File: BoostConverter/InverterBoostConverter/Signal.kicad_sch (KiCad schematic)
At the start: 58 parts, among them IC4 LM358DR, IC5 LM358DR, IC6 MCP2515-e_ST, IC7 TJA1050T_CM,118, SW1 SW_Push, U2 TL431AIDBZR, U4 TMP36xS, U5 TMP36xS, Y1 8MHz

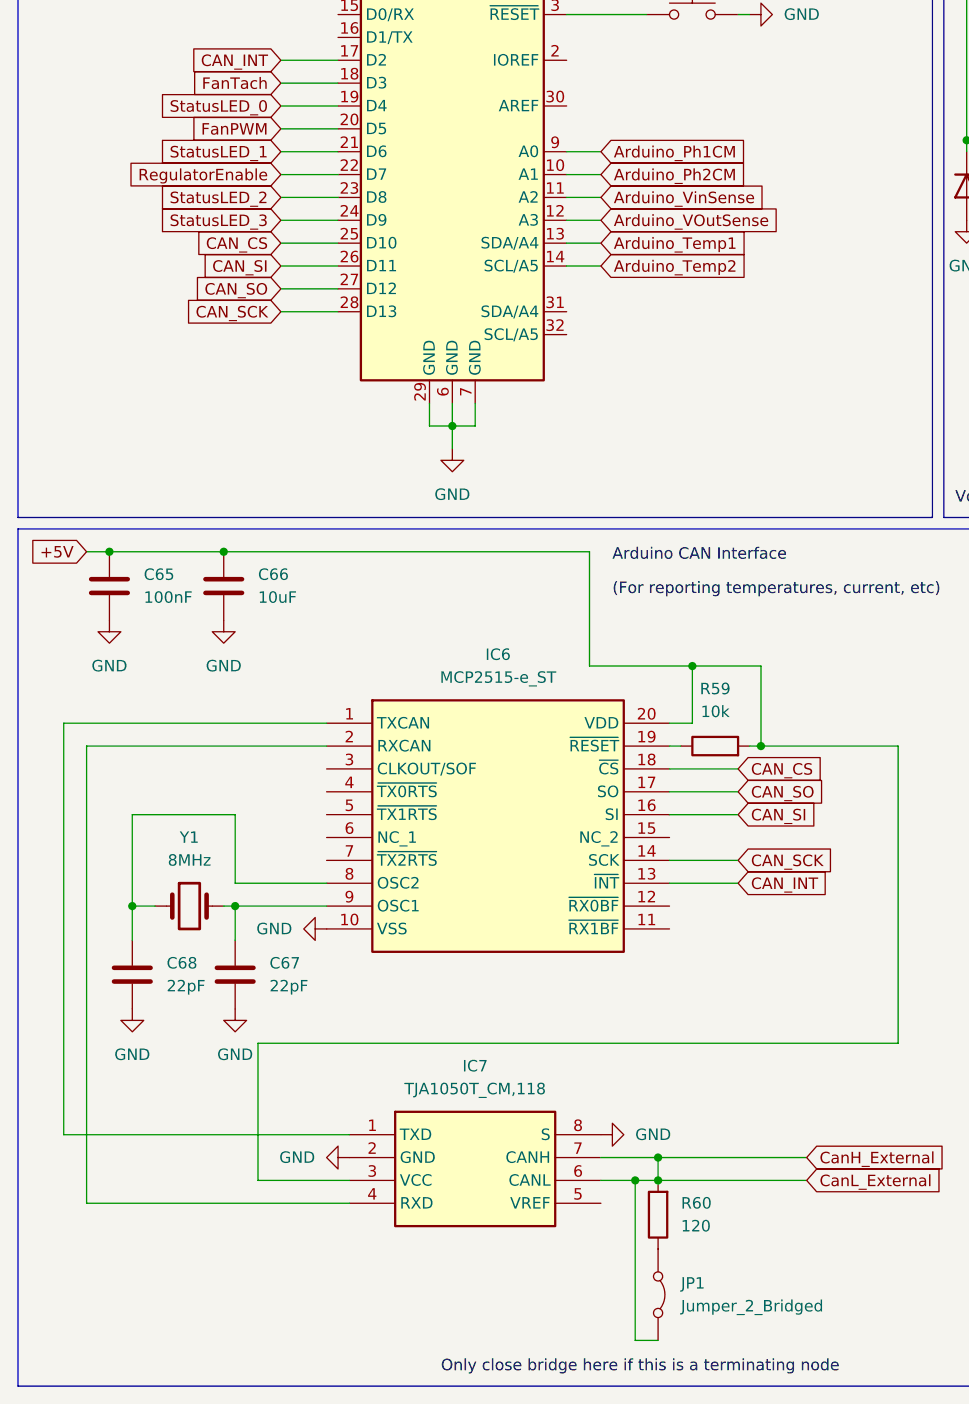
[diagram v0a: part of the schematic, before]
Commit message: Update boost converter, add inverter
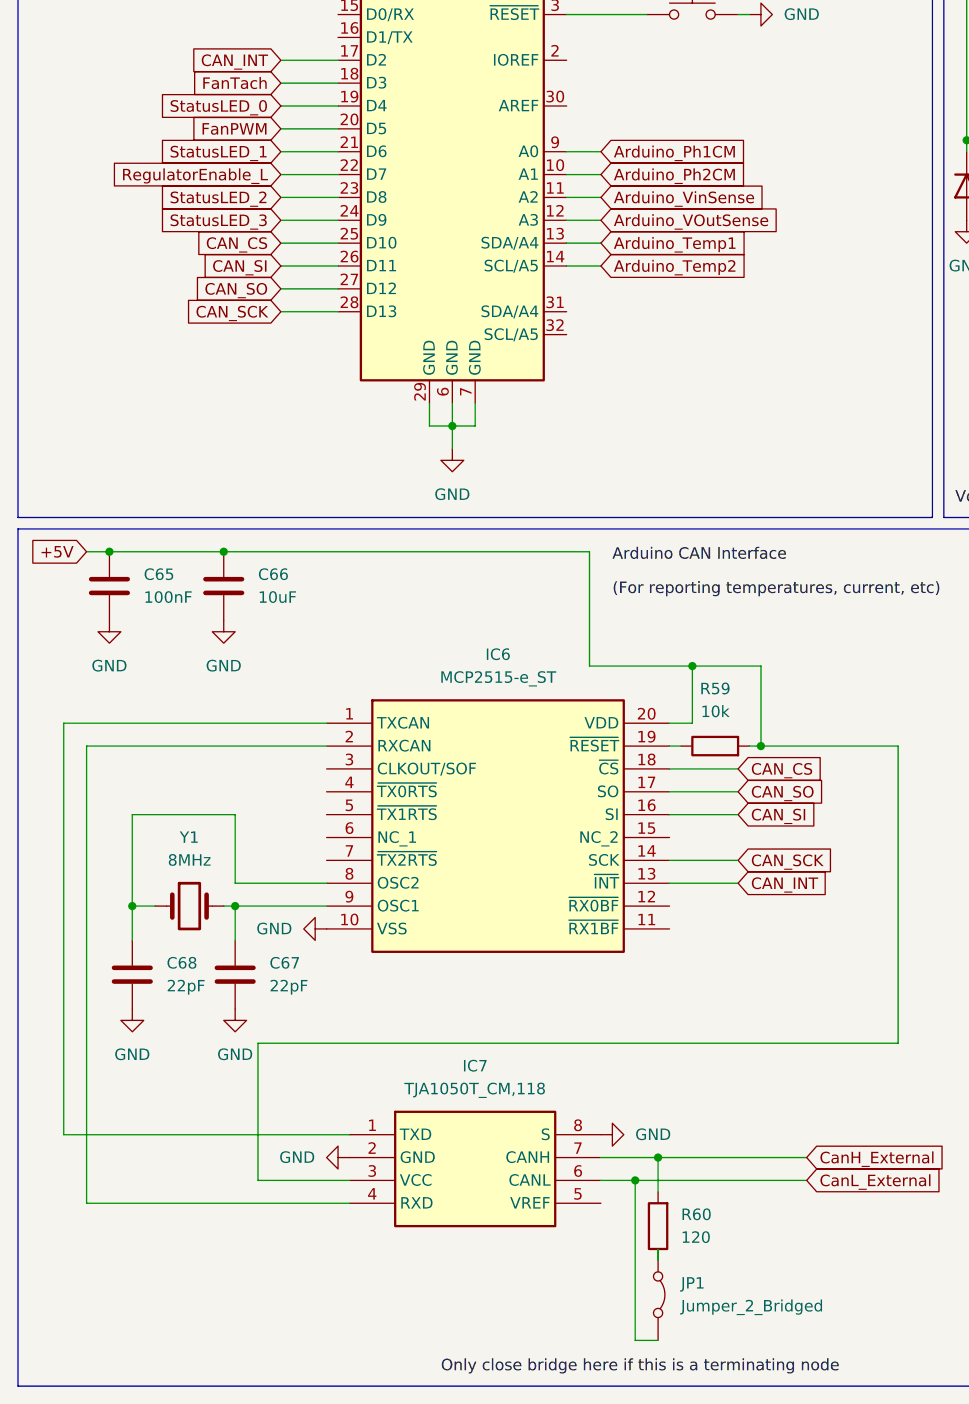
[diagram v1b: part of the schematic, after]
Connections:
- net CanH_External: no longer IC7.6 (CANL), JP1.2 (B)
- net RegulatorEnable renamed RegulatorEnable_L
- new net CanL_External: IC7.6 (CANL), JP1.2 (B)
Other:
- moved on the sheet: R60
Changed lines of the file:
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@@
 	)
 	(junction
-		(at 85.09 173.99)
-		(diameter 0)
-		(color 0 0 0 0)
-	)
-	(junction
 		(at 246.38 48.26)
 		(diameter 0)
@@
 	)
 	(junction
+		(at 85.09 171.45)
+		(diameter 0)
+		(color 0 0 0 0)
+	)
+	(junction
 		(at 278.13 48.26)
 		(diameter 0)
@@
 		(color 0 0 0 0)
 	)
-	(junction
-		(at 85.09 171.45)
-		(diameter 0)
-		(color 0 0 0 0)
-	)
 	(wire
 		(pts
@@
 	(wire
 		(pts
-			(xy 85.09 173.99) (xy 101.6 173.99)
-		)
-		(stroke
-			(width 0)
-			(type default)
-		)
-	)
-	(wire
-		(pts
 			(xy 78.74 17.78) (xy 91.44 17.78)
 		)
@@
 	(wire
 		(pts
+			(xy 85.09 171.45) (xy 101.6 171.45)
+		)
+		(stroke
+			(width 0)
+			(type default)
+		)
+	)
+	(wire
+		(pts
 			(xy 74.93 67.31) (xy 78.74 67.31)
 		)
@@
 	(wire
 		(pts
-			(xy 82.55 173.99) (xy 85.09 173.99)
+			(xy 82.55 173.99) (xy 101.6 173.99)
 		)
 		(stroke
@@
 	(wire
 		(pts
+			(xy 85.09 171.45) (xy 85.09 175.26)
+		)
+		(stroke
+			(width 0)
+			(type default)
+		)
+	)
+	(wire
+		(pts
 			(xy 43.18 57.15) (xy 49.53 57.15)
 		)
@@
 	(wire
 		(pts
-			(xy 85.09 171.45) (xy 101.6 171.45)
-		)
-		(stroke
-			(width 0)
-			(type default)
-		)
-	)
-	(wire
-		(pts
 			(xy 191.77 123.19) (xy 195.58 123.19)
 		)
@@
 	(wire
 		(pts
-			(xy 85.09 171.45) (xy 85.09 173.99)
+			(xy 129.54 52.07) (xy 129.54 58.42)
 		)
 		(stroke
@@
 	(wire
 		(pts
-			(xy 129.54 52.07) (xy 129.54 58.42)
+			(xy 193.04 134.62) (xy 195.58 134.62)
 		)
 		(stroke
@@
 	(wire
 		(pts
-			(xy 193.04 134.62) (xy 195.58 134.62)
+			(xy 156.21 125.73) (xy 158.75 125.73)
 		)
 		(stroke
@@
 	(wire
 		(pts
-			(xy 156.21 125.73) (xy 158.75 125.73)
+			(xy 180.34 36.83) (xy 180.34 60.96)
 		)
 		(stroke
@@
 	(wire
 		(pts
-			(xy 180.34 36.83) (xy 180.34 60.96)
+			(xy 236.22 123.19) (xy 240.03 123.19)
 		)
 		(stroke
@@
 	(wire
 		(pts
-			(xy 236.22 123.19) (xy 240.03 123.19)
+			(xy 21.59 104.14) (xy 24.13 104.14)
 		)
 		(stroke
@@
 	(wire
 		(pts
-			(xy 21.59 104.14) (xy 24.13 104.14)
+			(xy 85.09 182.88) (xy 85.09 181.61)
 		)
 		(stroke
@@
 		)
 	)
-	(global_label "RegulatorEnable"
-		(shape input)
-		(at 43.18 62.23 180)
-		(fields_autoplaced yes)
-		(effects
-			(font
-				(size 1.27 1.27)
-			)
-			(justify right)
-		)
-		(property "Intersheetrefs" "${INTERSHEET_REFS}"
-			(at 24.7133 62.23 0)
-			(effects
-				(font
-					(size 1.27 1.27)
-				)
-				(justify right)
-				(hide yes)
-			)
-		)
-	)
 	(global_label "CAN_SCK"
 		(shape input)
@@
 		)
 	)
+	(global_label "RegulatorEnable_L"
+		(shape input)
+		(at 43.18 62.23 180)
+		(fields_autoplaced yes)
+		(effects
+			(font
+				(size 1.27 1.27)
+			)
+			(justify right)
+		)
+		(property "Intersheetrefs" "${INTERSHEET_REFS}"
+			(at 22.7176 62.23 0)
+			(effects
+				(font
+					(size 1.27 1.27)
+				)
+				(justify right)
+				(hide yes)
+			)
+		)
+	)
 	(global_label "CAN_INT"
 		(shape input)
@@
 	(symbol
 		(lib_id "Device:R")
-		(at 85.09 177.8 180)
+		(at 85.09 179.07 180)
 		(unit 1)
 		(exclude_from_sim no)
@@
 		(fields_autoplaced yes)
 		(property "Reference" "R60"
-			(at 87.63 176.5299 0)
+			(at 87.63 177.7999 0)
 			(effects
 				(font
@@
 		)
 		(property "Value" "120"
-			(at 87.63 179.0699 0)
+			(at 87.63 180.3399 0)
 			(effects
 				(font
@@
 		)
 		(property "Footprint" "1210"
-			(at 86.868 177.8 90)
+			(at 86.868 179.07 90)
 			(effects
 				(font
@@
 		)
 		(property "Datasheet" "~"
-			(at 85.09 177.8 0)
+			(at 85.09 179.07 0)
 			(effects
 				(font
@@
 		)
 		(property "Description" "Resistor"
-			(at 85.09 177.8 0)
+			(at 85.09 179.07 0)
 			(effects
 				(font

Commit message: Finish Boost Converter
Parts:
- A1: footprint Module:Arduino_UNO_R3 -> InverterCom:Arduino_UNO_R3_ModifiedCourtyard
- C1: footprint CAPPRD500W60D1025H1750 -> InverterCom:CAPPRD500W60D1025H1750
- C28, C57, C58, C59, C60, C61, C62, C63, C64, C65, C66, C67, C68, C69, C70: footprint 1210 -> Capacitor_SMD:C_1210_3225Metric_Pad1.33x2.70mm_HandSolder
- IC4, IC5, IC7: footprint SOIC127P600X175-8N -> InverterCom:SOIC127P600X175-8N
- IC6: footprint SOP65P640X120-20N -> InverterCom:SOP65P640X120-20N
- JP1: footprint (none) -> Jumper:SolderJumper-3_P2.0mm_Open_TrianglePad1.0x1.5mm_NumberLabels
- LED1, LED2, LED3, LED4: footprint LEDC3216X120N -> InverterCom:LEDC3216X120N
- R27, R28, R29, R59, R60, R62, R63, R64, R71, R78, R79: footprint 1210 -> Resistor_SMD:R_1210_3225Metric_Pad1.30x2.65mm_HandSolder
- R65, R66, R67, R68, R69, R70, R72, R73, R74, R75, R76, R77: footprint RESC6431X65N -> InverterCom:RESC6431X65N
- SW1: footprint (none) -> Connector_Coaxial:SMA_Wurth_60312002114503_Vertical
- U2: footprint SOT95P237X112-3N -> InverterCom:SOT95P237X112-3N
- Y1: footprint (none) -> Crystal:Crystal_SMD_7050-2Pin_7.0x5.0mm_HandSoldering
- Z2, Z3, Z4, Z5: footprint SOD3716X135N -> InverterCom:SOD3716X135N
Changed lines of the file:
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@@
 			)
 		)
-		(property "Footprint" ""
+		(property "Footprint" "Jumper:SolderJumper-3_P2.0mm_Open_TrianglePad1.0x1.5mm_NumberLabels"
 			(at 85.09 186.69 0)
 			(effects
@@
 			)
 		)
-		(property "Footprint" "1210"
+		(property "Footprint" "Resistor_SMD:R_1210_3225Metric_Pad1.30x2.65mm_HandSolder"
 			(at 193.802 128.27 90)
 			(effects
@@
 			)
 		)
-		(property "Footprint" ""
+		(property "Footprint" "Crystal:Crystal_SMD_7050-2Pin_7.0x5.0mm_HandSoldering"
 			(at 33.02 143.51 0)
 			(effects
@@
 			)
 		)
-		(property "Footprint" "1210"
+		(property "Footprint" "Resistor_SMD:R_1210_3225Metric_Pad1.30x2.65mm_HandSolder"
 			(at 86.868 179.07 90)
 			(effects
@@
 			)
 		)
-		(property "Footprint" "SOD3716X135N"
+		(property "Footprint" "InverterCom:SOD3716X135N"
 			(at 132.08 33.02 0)
 			(effects
@@
 			)
 		)
-		(property "Footprint" "1210"
+		(property "Footprint" "Capacitor_SMD:C_1210_3225Metric_Pad1.33x2.70mm_HandSolder"
 			(at 157.1752 134.62 0)
 			(effects
@@
 			)
 		)
-		(property "Footprint" "Module:Arduino_UNO_R3"
+		(property "Footprint" "InverterCom:Arduino_UNO_R3_ModifiedCourtyard"
 			(at 62.23 59.69 0)
 			(effects
@@
 			)
 		)
-		(property "Footprint" "1210"
+		(property "Footprint" "Capacitor_SMD:C_1210_3225Metric_Pad1.33x2.70mm_HandSolder"
 			(at 79.7052 25.4 0)
 			(effects
@@
 			)
 		)
-		(property "Footprint" "1210"
+		(property "Footprint" "Capacitor_SMD:C_1210_3225Metric_Pad1.33x2.70mm_HandSolder"
 			(at 25.0952 111.76 0)
 			(effects
@@
 			)
 		)
-		(property "Footprint" "1210"
+		(property "Footprint" "Capacitor_SMD:C_1210_3225Metric_Pad1.33x2.70mm_HandSolder"
 			(at 133.0452 88.9 0)
 			(effects
@@
 			)
 		)
-		(property "Footprint" "RESC6431X65N"
+		(property "Footprint" "InverterCom:RESC6431X65N"
 			(at 223.52 -66.98 0)
 			(effects
@@
 			)
 		)
-		(property "Footprint" "1210"
+		(property "Footprint" "Resistor_SMD:R_1210_3225Metric_Pad1.30x2.65mm_HandSolder"
 			(at 274.32 50.038 90)
 			(effects
@@
 			)
 		)
-		(property "Footprint" "SOIC127P600X175-8N"
+		(property "Footprint" "InverterCom:SOIC127P600X175-8N"
 			(at 194.31 -14.91 0)
 			(effects
@@
 			)
 		)
-		(property "Footprint" "RESC6431X65N"
+		(property "Footprint" "InverterCom:RESC6431X65N"
 			(at 255.27 -73.33 0)
 			(effects
@@
 			)
 		)
-		(property "Footprint" "1210"
+		(property "Footprint" "Capacitor_SMD:C_1210_3225Metric_Pad1.33x2.70mm_HandSolder"
 			(at 92.4052 25.4 0)
 			(effects
@@
 			)
 		)
-		(property "Footprint" "SOP65P640X120-20N"
+		(property "Footprint" "InverterCom:SOP65P640X120-20N"
 			(at 82.55 218.11 0)
 			(effects
@@
 			)
 		)
-		(property "Footprint" "1210"
+		(property "Footprint" "Capacitor_SMD:C_1210_3225Metric_Pad1.33x2.70mm_HandSolder"
 			(at 210.5152 93.98 0)
 			(effects
@@
 			)
 		)
-		(property "Footprint" "RESC6431X65N"
+		(property "Footprint" "InverterCom:RESC6431X65N"
 			(at 255.27 -54.28 0)
 			(effects
@@
 			)
 		)
-		(property "Footprint" "1210"
+		(property "Footprint" "Capacitor_SMD:C_1210_3225Metric_Pad1.33x2.70mm_HandSolder"
 			(at 37.7952 111.76 0)
 			(effects
@@
 			)
 		)
-		(property "Footprint" "RESC6431X65N"
+		(property "Footprint" "InverterCom:RESC6431X65N"
 			(at 223.52 -73.33 0)
 			(effects
@@
 			)
 		)
-		(property "Footprint" "LEDC3216X120N"
+		(property "Footprint" "InverterCom:LEDC3216X120N"
 			(at 225.73 128.27 0)
 			(effects
@@
 			)
 		)
-		(property "Footprint" "1210"
+		(property "Footprint" "Capacitor_SMD:C_1210_3225Metric_Pad1.33x2.70mm_HandSolder"
 			(at 25.0952 25.4 0)
 			(effects
@@
 			)
 		)
-		(property "Footprint" "1210"
+		(property "Footprint" "Resistor_SMD:R_1210_3225Metric_Pad1.30x2.65mm_HandSolder"
 			(at 127.762 170.18 90)
 			(effects
@@
 			)
 		)
-		(property "Footprint" "1210"
+		(property "Footprint" "Capacitor_SMD:C_1210_3225Metric_Pad1.33x2.70mm_HandSolder"
 			(at 39.0652 154.94 0)
 			(effects
@@
 			)
 		)
-		(property "Footprint" "1210"
+		(property "Footprint" "Resistor_SMD:R_1210_3225Metric_Pad1.30x2.65mm_HandSolder"
 			(at 130.302 121.92 90)
 			(effects
@@
 			)
 		)
-		(property "Footprint" "LEDC3216X120N"
+		(property "Footprint" "InverterCom:LEDC3216X120N"
 			(at 238.43 176.53 0)
 			(effects
@@
 			)
 		)
-		(property "Footprint" "1210"
+		(property "Footprint" "Capacitor_SMD:C_1210_3225Metric_Pad1.33x2.70mm_HandSolder"
 			(at 199.0852 93.98 0)
 			(effects
@@
 			)
 		)
-		(property "Footprint" "LEDC3216X120N"
+		(property "Footprint" "InverterCom:LEDC3216X120N"
 			(at 253.67 176.53 0)
 			(effects
@@
 			)
 		)
-		(property "Footprint" "LEDC3216X120N"
+		(property "Footprint" "InverterCom:LEDC3216X120N"
 			(at 223.19 176.53 0)
 			(effects
@@
 			)
 		)
-		(property "Footprint" "1210"
+		(property "Footprint" "Resistor_SMD:R_1210_3225Metric_Pad1.30x2.65mm_HandSolder"
 			(at 193.802 118.11 90)
 			(effects
@@
 			)
 		)
-		(property "Footprint" "1210"
+		(property "Footprint" "Resistor_SMD:R_1210_3225Metric_Pad1.30x2.65mm_HandSolder"
 			(at 158.242 170.18 90)
 			(effects
@@
 			)
 		)
-		(property "Footprint" "1210"
+		(property "Footprint" "Capacitor_SMD:C_1210_3225Metric_Pad1.33x2.70mm_HandSolder"
 			(at 27.6352 154.94 0)
 			(effects
@@
 			)
 		)
-		(property "Footprint" "SOD3716X135N"
+		(property "Footprint" "InverterCom:SOD3716X135N"
 			(at 194.31 34.29 0)
 			(effects
@@
 			)
 		)
-		(property "Footprint" "RESC6431X65N"
+		(property "Footprint" "InverterCom:RESC6431X65N"
 			(at 255.27 -60.63 0)
 			(effects
@@
 			)
 		)
-		(property "Footprint" "1210"
+		(property "Footprint" "Resistor_SMD:R_1210_3225Metric_Pad1.30x2.65mm_HandSolder"
 			(at 154.432 140.97 90)
 			(effects
@@
 			)
 		)
-		(property "Footprint" "SOD3716X135N"
+		(property "Footprint" "InverterCom:SOD3716X135N"
 			(at 180.34 71.12 0)
 			(effects
@@
 			)
 		)
-		(property "Footprint" "1210"
+		(property "Footprint" "Capacitor_SMD:C_1210_3225Metric_Pad1.33x2.70mm_HandSolder"
 			(at 246.38 37.1348 0)
 			(effects
@@
 			)
 		)
-		(property "Footprint" "1210"
+		(property "Footprint" "Resistor_SMD:R_1210_3225Metric_Pad1.30x2.65mm_HandSolder"
 			(at 143.002 170.18 90)
 			(effects
@@
 			)
 		)
-		(property "Footprint" "RESC6431X65N"
+		(property "Footprint" "InverterCom:RESC6431X65N"
 			(at 255.27 -47.93 0)
 			(effects
@@
 			)
 		)
-		(property "Footprint" "1210"
+		(property "Footprint" "Capacitor_SMD:C_1210_3225Metric_Pad1.33x2.70mm_HandSolder"
 			(at 278.13 37.1348 0)
 			(effects
@@
 			)
 		)
-		(property "Footprint" "SOD3716X135N"
+		(property "Footprint" "InverterCom:SOD3716X135N"
 			(at 119.38 63.5 0)
 			(effects
@@
 			)
 		)
-		(property "Footprint" "1210"
+		(property "Footprint" "Resistor_SMD:R_1210_3225Metric_Pad1.30x2.65mm_HandSolder"
 			(at 91.44 127.508 90)
 			(effects
@@
 			)
 		)
-		(property "Footprint" "RESC6431X65N"
+		(property "Footprint" "InverterCom:RESC6431X65N"
 			(at 223.52 -54.28 0)
 			(effects
@@
 			)
 		)
-		(property "Footprint" "RESC6431X65N"
+		(property "Footprint" "InverterCom:RESC6431X65N"
 			(at 223.52 -47.93 0)
 			(effects
@@
 			)
 		)
-		(property "Footprint" "1210"
+		(property "Footprint" "Resistor_SMD:R_1210_3225Metric_Pad1.30x2.65mm_HandSolder"
 			(at 242.57 50.038 90)
 			(effects
@@
 			)
 		)
-		(property "Footprint" "RESC6431X65N"
+		(property "Footprint" "InverterCom:RESC6431X65N"
 			(at 255.27 -66.98 0)
 			(effects
@@
 			)
 		)
-		(property "Footprint" "RESC6431X65N"
+		(property "Footprint" "InverterCom:RESC6431X65N"
 			(at 223.52 -60.63 0)
 			(effects
@@
 			)
 		)
-		(property "Footprint" "RESC6431X65N"
+		(property "Footprint" "InverterCom:RESC6431X65N"
 			(at 223.52 -79.68 0)
 			(effects
@@
 			)
 		)
-		(property "Footprint" "SOIC127P600X175-8N"
+		(property "Footprint" "InverterCom:SOIC127P600X175-8N"
 			(at 133.35 -23.8 0)
 			(effects
@@
 			)
 		)
-		(property "Footprint" ""
+		(property "Footprint" "Connector_Coaxial:SMA_Wurth_60312002114503_Vertical"
 			(at 88.9 39.37 0)
 			(effects
@@
 			)
 		)
-		(property "Footprint" "1210"
+		(property "Footprint" "Capacitor_SMD:C_1210_3225Metric_Pad1.33x2.70mm_HandSolder"
 			(at 37.7952 25.4 0)
 			(effects
@@
 			)
 		)
-		(property "Footprint" "SOT95P237X112-3N"
+		(property "Footprint" "InverterCom:SOT95P237X112-3N"
 			(at 162.56 30.81 0)
 			(effects
@@
 			)
 		)
-		(property "Footprint" "SOIC127P600X175-8N"
+		(property "Footprint" "InverterCom:SOIC127P600X175-8N"
 			(at 74.93 263.83 0)
 			(effects
@@
 			)
 		)
-		(property "Footprint" "1210"
+		(property "Footprint" "Capacitor_SMD:C_1210_3225Metric_Pad1.33x2.70mm_HandSolder"
 			(at 144.4752 88.9 0)
 			(effects
@@
 			)
 		)
-		(property "Footprint" "CAPPRD500W60D1025H1750"
+		(property "Footprint" "InverterCom:CAPPRD500W60D1025H1750"
 			(at -47.93 26.67 0)
 			(effects
@@
 			)
 		)
-		(property "Footprint" "RESC6431X65N"
+		(property "Footprint" "InverterCom:RESC6431X65N"
 			(at 255.27 -79.68 0)
 			(effects

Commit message: Update boost converter layout
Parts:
- added C4, C5: 1uF, Capacitor_SMD:C_1210_3225Metric_Pad1.33x2.70mm_HandSolder, symbol Device:C
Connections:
- net +5V: now also C4.1, C5.1
- net GND: now also C4.2, C5.2
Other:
- moved on the sheet: U4, U5

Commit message: udpate
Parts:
- R70, R77: value 1M -> RC2512JK-071ML
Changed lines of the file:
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@@
 			)
 		)
-		(property "Value" "1M"
+		(property "Value" "RC2512JK-071ML"
 			(at 259.0801 50.8 90)
 			(effects
@@
 			)
 		)
-		(property "Value" "1M"
+		(property "Value" "RC2512JK-071ML"
 			(at 227.3301 50.8 90)
 			(effects
